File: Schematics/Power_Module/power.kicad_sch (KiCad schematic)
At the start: 79 parts, among them J2 ScrewSwitch, J3 Battery, J6 ScrewSwitch, J7 GSE, Q1 AO4447A, Q3 TSM2309CX, Q5 DMN6040SSD-13, U1 LMR51430XDDCR, U10 TPS61175PWPR, U14 LM74700QDBVRQ1, U15 LM74700QDBVRQ1, U2 LMR51430XDDCR, U3 ACS37041KLHBLT-010B3, U4 AMS1117-3.3, U5 ACS37041KLHBLT-010B3, U6 LM66100DCKR, U7 LM66100DCKR, U8 LM66100DCKR

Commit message: finalized buck and boost designs,
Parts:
- C36: value C -> 33nF; LCSC (none) -> C21117
- C37, C38: value C -> 10uF; footprint (none) -> Capacitor_SMD:C_1206_3216Metric; LCSC (none) -> C13585
- D8: value D_Schottky -> 50V 3A; footprint (none) -> Diode_SMD:D_SMA; Digikey (none) -> 112-VSSAF5N50-M3/6BCT-ND
- L1: value 27uH -> 22uH; Digikey 118-SRR1260A-270MTR-ND -> SRR1260A-220MCT-ND
- L2: value 120uH -> 68uH; Digikey SRR1260A-121KCT-ND -> 118-SRR1260A-680MCT-ND
- L3: value L -> 47uH; footprint (none) -> Inductor_SMD:L_Bourns_SRR1260; Digikey (none) -> SRR1260A-470MCT-ND
- R23: value R -> 6.2k; LCSC (none) -> C4260
- R26: value R -> 82K; LCSC (none) -> C23254
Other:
- note added: "Max Output: 2.1A Inductor limited"
- note added: "Need to verify COMP resiter & capcitor"
- note removed: "Max Output: 1.65A Inductor limited"
- note removed: "Need to decide frequency resister, inductance, output capacitance, diode, and COMP resiter & capcitor"
- moved on the sheet: C33, C34, C35, C36, C37, C38, C39, C40, C41, C42, C43, C45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

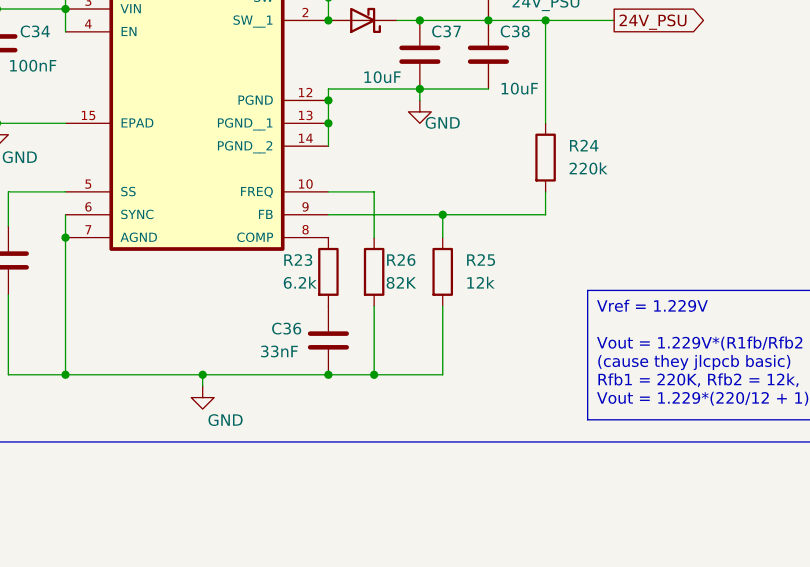
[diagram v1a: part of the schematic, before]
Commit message: minor review of part numbers  - NEED major review of buck and boost design
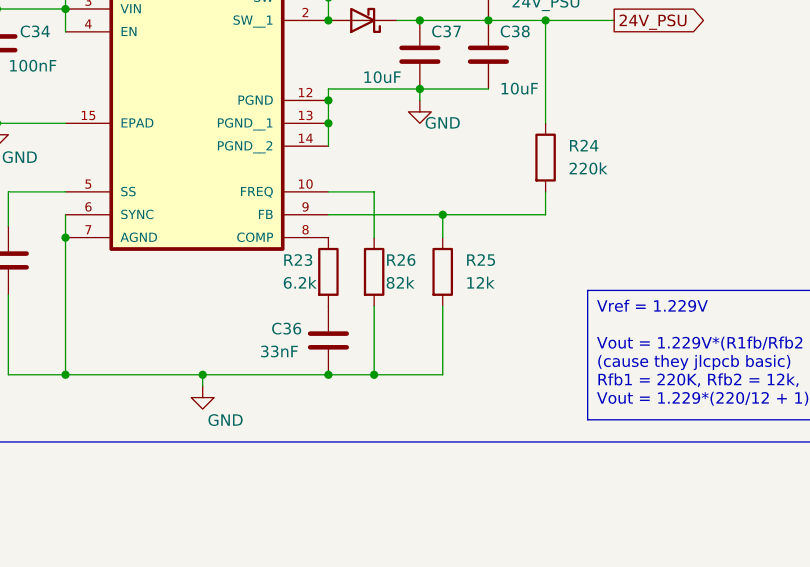
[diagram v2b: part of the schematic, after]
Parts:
- C36: footprint (none) -> Capacitor_SMD:C_0603_1608Metric
- R23: footprint (none) -> Resistor_SMD:R_0603_1608Metric
- R26: value 82K -> 82k; footprint (none) -> Resistor_SMD:R_0603_1608Metric
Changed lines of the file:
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@@
 			)
 		)
-		(property "Footprint" ""
+		(property "Footprint" "Resistor_SMD:R_0603_1608Metric"
 			(at 244.602 161.29 90)
 			(effects
@@
 			)
 		)
-		(property "Footprint" ""
+		(property "Footprint" "Capacitor_SMD:C_0603_1608Metric"
 			(at 247.3452 172.72 0)
 			(effects
@@
 			)
 		)
-		(property "Value" "82K"
+		(property "Value" "82k"
 			(at 252.73 162.56 0)
 			(effects
@@
 			)
 		)
-		(property "Footprint" ""
+		(property "Footprint" "Resistor_SMD:R_0603_1608Metric"
 			(at 249.682 161.29 90)
 			(effects

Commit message: started layout design  - added shunt based 24V current sensing
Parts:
- added C13, C17: 100nF, Capacitor_SMD:C_0603_1608Metric, symbol Device:C
- added C14: 4.7uF, Capacitor_SMD:C_0805_2012Metric, symbol Device:C
- added D7: 24V PWR (YLW), LED_SMD:LED_0805_2012Metric, symbol Device:LED
- added R12: 1k, Resistor_SMD:R_0603_1608Metric, symbol Device:R
- added R14: 10k, Resistor_SMD:R_0603_1608Metric, symbol Device:R
- added R15: 100k, Resistor_SMD:R_0603_1608Metric, symbol Device:R
- added R6: 0.1, Resistor_SMD:R_1206_3216Metric_Pad1.30x1.75mm_HandSolder, symbol Device:R
- added R7: 30k, Resistor_SMD:R_0603_1608Metric, symbol Device:R
- added TP4: 24V_MUX, TestPoint:TestPoint_Pad_2.0x2.0mm, symbol Connector:TestPoint
- added TP9: 24VSENS, TestPoint:TestPoint_Pad_1.5x1.5mm, symbol Connector:TestPoint
- added U6: INA181A2, Package_TO_SOT_SMD:SOT-23-6, symbol Amplifier_Current:INA181
- C11: renamed from C38; JLCPCB (none) -> C13585; LCSC C13585 -> (none)
- C15: renamed from C9; value 0.1u -> 100nF
- C16: renamed from C10; value 0.1u -> 100nF
- C8: renamed from C36; JLCPCB (none) -> C21117; LCSC C21117 -> (none)
- C9: renamed from C37; JLCPCB (none) -> C13585; LCSC C13585 -> (none)
- D1: renamed from D5; JLCPCB (none) -> C113965; LCSC C113965 -> (none)
- D2: renamed from D6; JLCPCB (none) -> C113965; LCSC C113965 -> (none)
- D3: renamed from D7; JLCPCB (none) -> C545360; LCSC C545360 -> (none)
- D5: renamed from D1; value 3.3V_A PWR (GRN) -> 3.3V PWR (GRN)
- D6: renamed from D2; value 5V_A PWR (RED) -> 5V PWR (RED)
- L1: renamed from L3; footprint Inductor_SMD:L_Bourns_SRR1260 -> Inductor_SMD:L_Bourns_SRN8040TA; Digikey SRR1260A-470MCT-ND -> 283-SDCHA1V8040-470-RCT-ND
- L2: renamed from L1; footprint Inductor_SMD:L_Bourns_SRR1260 -> Inductor_SMD:L_Bourns_SRN8040TA; Digikey SRR1260A-220MCT-ND -> 283-SDCHA1V8040-220-RCT-ND
- L3: renamed from L2; footprint Inductor_SMD:L_Bourns_SRR1260 -> Inductor_SMD:L_Bourns_SRN8040TA; Digikey 118-SRR1260A-680MCT-ND -> 283-SDCHA1V8040-680-RCT-ND
- Q2: renamed from Q3; JLCPCB (none) -> C2977534; LCSC C2977534 -> (none)
- Q3: renamed from Q5; JLCPCB (none) -> C154876; LCSC C154876 -> (none)
- R1: renamed from R23; JLCPCB (none) -> C4260; LCSC C4260 -> (none)
- R10: value 30k -> 12K; JLCPCB C22984 -> C22790
- R2: renamed from R26; JLCPCB (none) -> C23254; LCSC C23254 -> (none)
- R3: renamed from R25; JLCPCB (none) -> C22790; LCSC C22790 -> (none)
- R4: renamed from R24; JLCPCB (none) -> C22961; LCSC C22961 -> (none)
- U1: renamed from U10; footprint TPS61175PWPR:IC_TPS27S100BPWPR -> footprints:IC_TPS27S100BPWPR; JLCPCB (none) -> C43276; LCSC C43276 -> (none)
- U2: renamed from U15; JLCPCB (none) -> C2941042; LCSC C2941042 -> (none)
- U3: renamed from U14; JLCPCB (none) -> C2941042; LCSC C2941042 -> (none)
- U5: value ACS37041KLHBLT-010B3 -> ACS37041KLHBLT-010B5; Digikey 620-ACS37041KLHBLT-010B3CT-ND -> 620-ACS37041KLHBLT-010B5CT-ND
- U7: renamed from U1; JLCPCB (none) -> C5185863; LCSC C5185863 -> (none)
- U8: renamed from U2; JLCPCB (none) -> C5185863; LCSC C5185863 -> (none)
- renumbered C33 to C1, C45 to C10, C40 to C12, C1 to C18, C2 to C19, C34 to C2, C3 to C20, C4 to C21, C5 to C22, C6 to C23, C7 to C24, C8 to C25, C25 to C26, C24 to C27, C11 to C28, C12 to C29, C35 to C3, C13 to C30, C14 to C31, C15 to C32, C43 to C4, C42 to C5, C41 to C6, C39 to C7, D8 to D4, J2 to J1, J3 to J2, J6 to J3, J7 to J4, R5 to R11, R9 to R13, R1 to R16, R2 to R17, R3 to R18, R4 to R19, R6 to R5, R7 to R8, R8 to R9, TP2 to TP1, TP3 to TP10, TP4 to TP11, TP9 to TP2, TP1 to TP3, TP8 to TP5, TP7 to TP6, TP5 to TP7, TP6 to TP8, U7 to U10, U8 to U11, U4 to U12, U3 to U4, U6 to U9
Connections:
- net 24V_GSE: now also R14.2
- net 24V_MUX: now also R10.1, R6.2, U6.4 (-); no longer C10.1, C12.1, Q3.5 (D2), Q3.6 (D2), Q3.7 (D1), Q3.8 (D1), U2.4 (CATHODE), U3.4 (CATHODE)
- net 3.3V_MUX: now also C13.1, C14.1, U6.6 (V+)
- net 5V_SENSE: now also R7.1; no longer R10.1
- net GND: now also C13.2, C14.2, C17.2, D7.1 (K), R15.2, R7.2, U6.2 (GND), U6.5 (REF); no longer R10.2
- new net: R12.2, U6.1
- new net: D7.2 (A), R10.2
- new net 24V_CURR_SENSE: C17.1, R12.1
- new net 24V_MUX_Pre: C10.1, C12.1, Q3.5 (D2), Q3.6 (D2), Q3.7 (D1), Q3.8 (D1), R6.1, TP4.1, U2.4 (CATHODE), U3.4 (CATHODE), U6.3 (+)
- new net GSE_SENSE: R14.1, R15.1, TP9.1
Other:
- note added: "FOLLOW LAYOUT EXAMPLE (9.4.2) FROM DATASHEET LMR51430: PFM @ 500KHz (simpler routing & higher efficiency)"
- note added: "Vin=24V, Vf=2.8V, I=1.8mA, R=12k"
- note added: "Vin=3.3V, Vf=2.8V, I=0.15mA, R=3.3k"
- note removed: "Add 24V_GSE current and voltage sense!"
- note removed: "Add 24V_PSU current and voltage sense!"
- note removed: "FOLLOW LAYOUT EXAMPLE (9.4.2) FROM DATASHEET LMR51430: PFM @ 1.1MHz (simpler routing & higher efficiency)"
- note removed: "Vin=3.3V, Vf=2.8V, R=0.15mA, R=3.3k"
- moved on the sheet: C1, C10, C11, C12, C15, C16, C18, C19, C2, C20, C21, C22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

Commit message: current progress on power board
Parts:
- added C37: 10uF, Capacitor_SMD:CP_Elec_4x5.4, symbol Device:C_Polarized
- TP9: value 24VSENS -> GSE_SENS
- U10, U11, U9: footprint LMR66100:SC-70-6_Handsoldering -> LMR66100:SC-70-6
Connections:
- net 3.3V_MUX: now also C37.1
- net GND: now also C37.2
- net BOOST_SW: now reaches D4.2 (A), L1.2, U1.1 (SW), U1.2 (SW__1)
- net GSE_SW+: now reaches D1.1 (A1), J3.2, Q2.3 (D)
- net BATT+: now reaches J1.1, J2.2
- net BATT_SW+: now reaches J1.2, Q1.5 (D), Q1.6 (D), Q1.7 (D), Q1.8 (D)
- net GSE+: now reaches J3.1, J4.2
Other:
- moved on the sheet: C28, C29, C30, Q1, TP1, U10, U11, U9

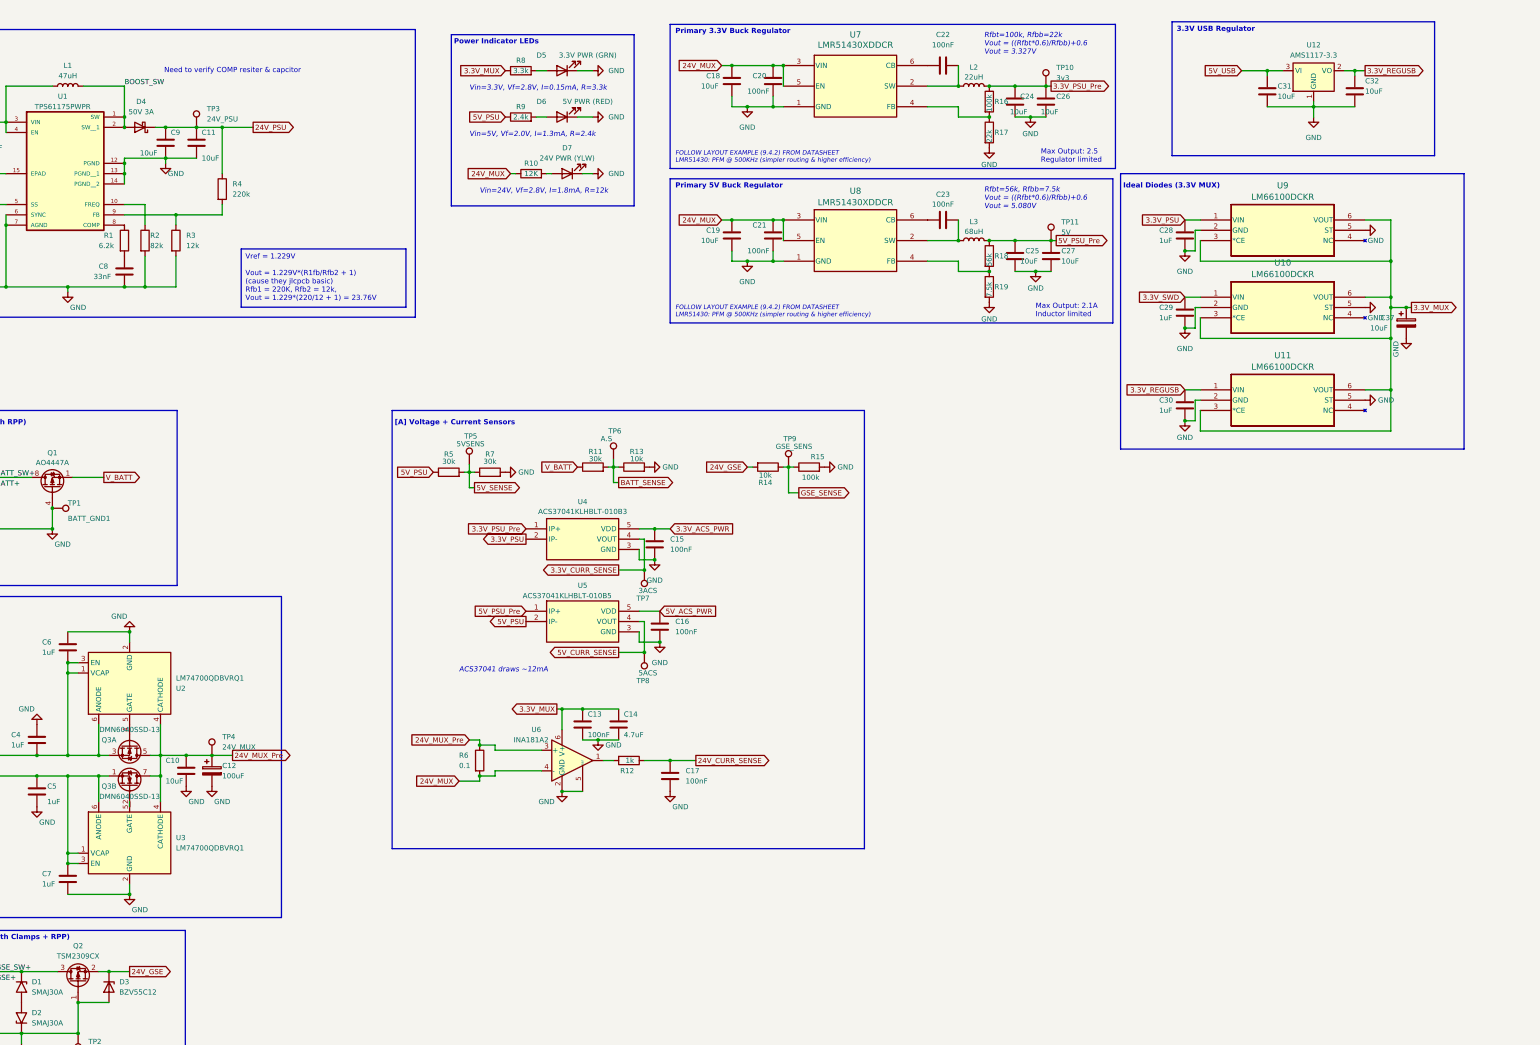
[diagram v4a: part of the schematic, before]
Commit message: major layout progress, still need to place MCU
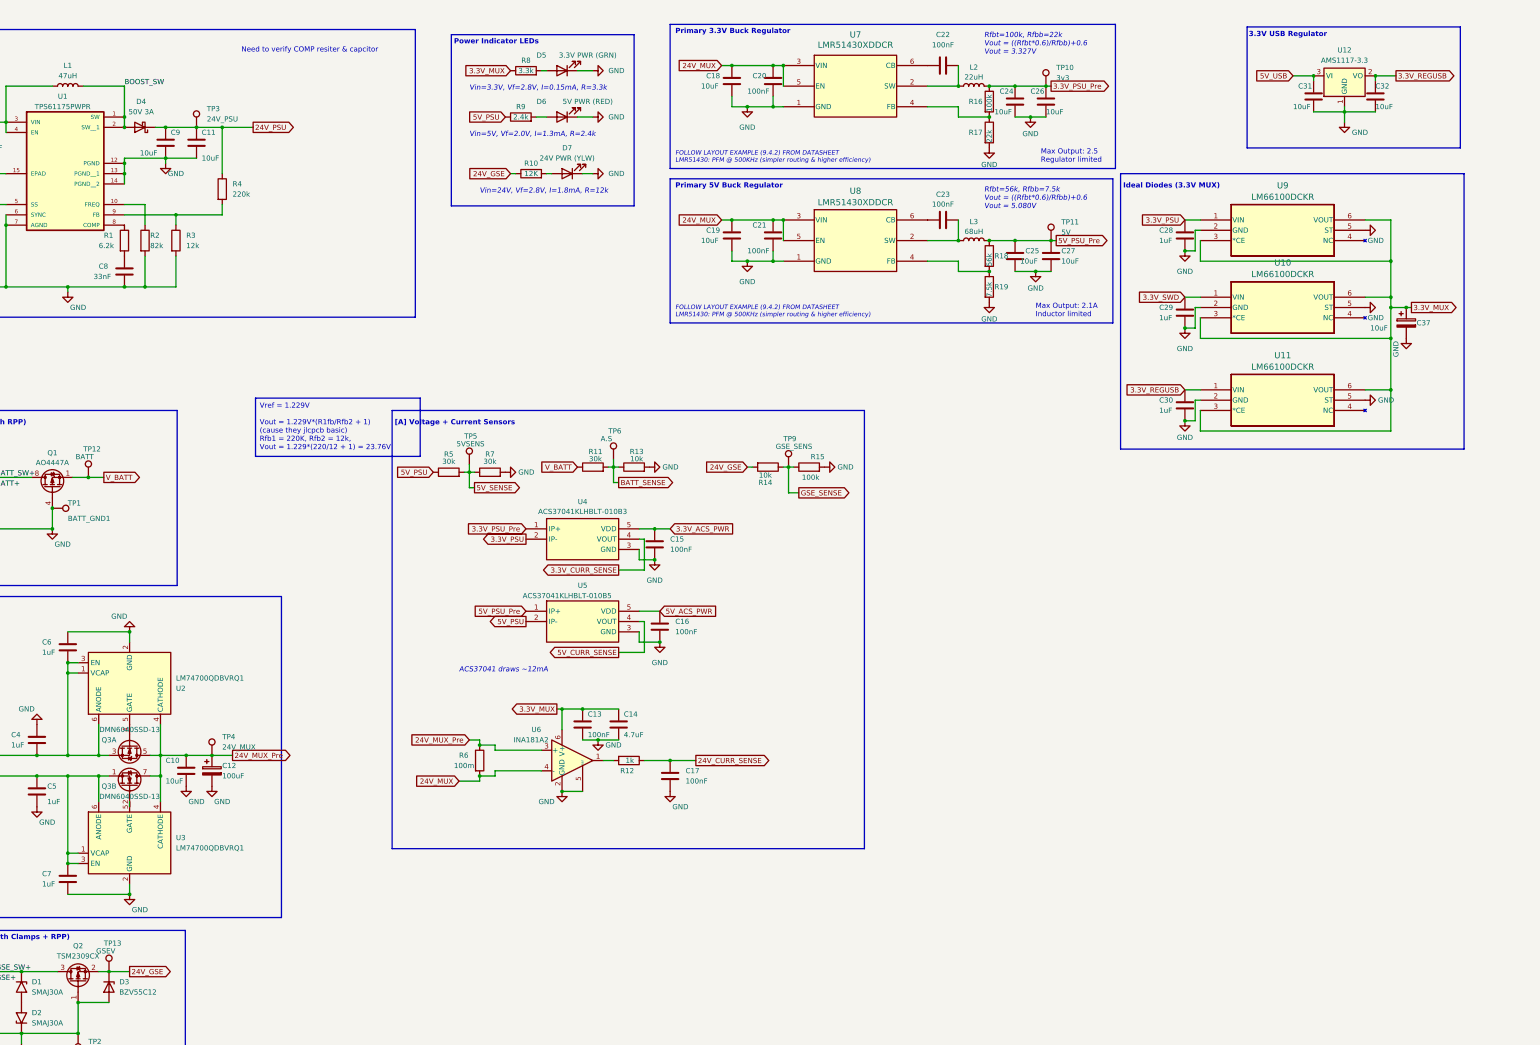
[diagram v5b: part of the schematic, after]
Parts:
- removed TP7: 3ACS, TestPoint:TestPoint_Pad_1.5x1.5mm, symbol Connector:TestPoint
- removed TP8: 5ACS, TestPoint:TestPoint_Pad_1.5x1.5mm, symbol Connector:TestPoint
- added TP12: BATT, TestPoint:TestPoint_Pad_1.5x1.5mm, symbol Connector:TestPoint
- added TP13: GSEV, TestPoint:TestPoint_Pad_1.5x1.5mm, symbol Connector:TestPoint
- R6: value 0.1 -> 100m; Digikey 273-KDV12DR100ETCT-ND -> P18940CT-ND
- TP1, TP10, TP11, TP2, TP3, TP4: footprint TestPoint:TestPoint_Pad_2.0x2.0mm -> TestPoint:TestPoint_Pad_1.5x1.5mm
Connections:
- net 24V_GSE: now also R10.1, TP13.1
- net 24V_MUX: no longer R10.1
- net V_BATT: now also TP12.1
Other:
- moved on the sheet: C31, C32, R8, U12

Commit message: continueing layout, confirmed all devices will fix  - need to add bulk rail caps  - fixed issue in oring logic
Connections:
- net 24V_GSE: no longer U3.1 (VCAP)
- net 24V_PSU: no longer U2.1 (VCAP)
- net GND: no longer C6.1, C7.2
- new net: C6.1, U2.1 (VCAP)
- new net: C7.2, U3.1 (VCAP)
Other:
- note added: "****Need to verify COMP resiter & capcitor"
- note added: "- TVS: clamps pos and neg rails (breakdown 31.1V) - P-MOSFET: RPP switch, VGS_max = +-20V - 12V ZENER: reverse bias Vgs = 0 - 12 = -12V, forward bias Vgs = 24 - 23.3 = 0.7v - can the zener handle the current?"
- note removed: "- TVS: clamps pos and neg rails (breakdown 31.1V) - P-MOSFET: RPP switch, VGS_max = +-20V - 12V ZENER: reverse bias Vgs = 0 - 12 = -12V, forward bias Vgs = 24 - 23.3 = 0.7v - can the zener handle the current"
- note removed: "Need to verify COMP resiter & capcitor"
- moved on the sheet: C1, C10, C11, C12, C13, C14, C15, C16, C17, C2, C3, C4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

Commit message: completed all power traces, finalizing signal traces
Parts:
- removed C12: 100uF, Capacitor_SMD:CP_Elec_6.3x5.9, symbol Device:C_Polarized
- removed C37: 10uF, Capacitor_SMD:CP_Elec_4x5.4, symbol Device:C_Polarized
- added C12, C51: 22uF, Capacitor_SMD:C_1206_3216Metric, symbol Device:C
- added C37: 10uF, Capacitor_SMD:C_0805_2012Metric, symbol Device:C
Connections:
- net 24V_MUX_Pre: now also C12.1, C51.1
- net 3.3V_MUX: now also C37.1
- net GND: now also C12.2, C37.2, C51.2
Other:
- moved on the sheet: C10, C4, C5, C6, C7, Q3A, Q3B, TP4, U2, U3

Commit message: finished all traces, confirmed major DRC errors  - need to fix silkscreen  - review needed and LCSC verification
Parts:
- removed TP10: 3v3, TestPoint:TestPoint_Pad_1.5x1.5mm, symbol Connector:TestPoint
- removed TP11: 5V, TestPoint:TestPoint_Pad_1.5x1.5mm, symbol Connector:TestPoint
- added TP7: 3v3, TestPoint:TestPoint_Pad_1.5x1.5mm, symbol Connector:TestPoint
- added TP8: 5V, TestPoint:TestPoint_Pad_1.5x1.5mm, symbol Connector:TestPoint
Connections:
- net 24V_MUX: now also TP4.1
- net 24V_MUX_Pre: no longer TP4.1
- net 3.3V_PSU: now also TP7.1
- net 5V_PSU: now also TP8.1
